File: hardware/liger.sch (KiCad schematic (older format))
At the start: 71 parts, among them P1 CONN_01X10, P2 CONN_01X10, P3 USB_OTG, P4 CONN_01X02, P5 CONN_01X04, Q1 Q_NMOS_GSD, Q2 Q_PMOS_GSD, Q3 Q_NPN_BEC, Q4 Q_NPN_BEC, SW1 SW_PUSH, U1 electret_microphone, U11 SPX3819, U2 ADA4075, U3 ESP-WROOM-02, U4 FT230XS, U5 PT5529B/L2/H2-F

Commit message: update
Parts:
- removed C?: 150nF, Capacitors_ThroughHole:C_Rect_L18_W6_H12_P15, symbol C
- removed R?: 1M, Resistors_ThroughHole:Resistor_Horizontal_RM15mm, symbol R
- removed R?: 68k, Resistors_ThroughHole:Resistor_Horizontal_RM15mm, symbol R
- removed R?: 33k, Resistors_ThroughHole:Resistor_Horizontal_RM15mm, symbol R
- removed R?: 6.8, Resistors_ThroughHole:Resistor_Horizontal_RM15mm, symbol R
- removed U?: common-mode-choke, symbol common-mode-choke
- added C? (x2): 12uF, Capacitors_ThroughHole:C_Radial_D10_L13_P5, symbol CP1
- added L?: BEAD, Resistors_SMD:R_0805_HandSoldering, symbol BK0603HS330-T
- added L?: 470uH, Capacitors_ThroughHole:C_Radial_D10_L13_P5, symbol BK0603HS330-T
- added R?: 0.91, Resistors_SMD:R_0805_HandSoldering, symbol R
- added R?: 0.82, Resistors_SMD:R_0805_HandSoldering, symbol R
- added RT?: 5, Resistors_ThroughHole:Resistor_Horizontal_RM10mm, symbol R
- BR?: renamed from D?; value Diode_Bridge -> DF08S; footprint (none) -> tba; Part Number (none) -> DF08S
- C?: value 150nF -> 330pF; footprint Capacitors_ThroughHole:C_Rect_L18_W6_H12_P15 -> Capacitors_SMD:C_0805_HandSoldering
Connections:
- wire segments 201 -> 200
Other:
- moved on the sheet: BR?, C?, D?

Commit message: update
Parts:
- C?: footprint Capacitors_ThroughHole:C_Radial_D16_L31.5_P7.5 -> Capacitors_ThroughHole:C_Radial_D10_L20_P7.5; Part Number (none) -> UPZ2G101MHD
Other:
- moved on the sheet: C?, D?
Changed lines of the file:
@@
 L C C?
 U 1 1 57C8658B
-P 5050 6650
-F 0 "C?" H 5150 6750 50  0000 L CNN
-F 1 "330pF" H 5100 6550 50  0000 L CNN
-F 2 "Capacitors_SMD:C_0805_HandSoldering" H 5165 6605 50  0001 L CNN
-F 3 "http://www.digikey.com/product-detail/en/kemet/C0805C331KCRACTU/399-7151-1-ND/3439391" H 5165 6514 50  0001 L CNN
-	1    5050 6650
+P 12400 7550
+F 0 "C?" H 12500 7650 50  0000 L CNN
+F 1 "330pF" H 12450 7450 50  0000 L CNN
+F 2 "Capacitors_SMD:C_0805_HandSoldering" H 12515 7505 50  0001 L CNN
+F 3 "http://www.digikey.com/product-detail/en/kemet/C0805C331KCRACTU/399-7151-1-ND/3439391" H 12515 7414 50  0001 L CNN
+	1    12400 7550
 	-1   0    0    1
 $EndComp
@@
 L CP1 C?
 U 1 1 57C87C6C
-P 8050 7600
-F 0 "C?" H 8165 7646 50  0000 L CNN
-F 1 "100uF" H 8165 7555 50  0000 L CNN
-F 2 "Capacitors_ThroughHole:C_Radial_D16_L31.5_P7.5" H 8165 7555 50  0001 L CNN
-F 3 "http://www.mouser.com/Search/ProductDetail.aspx?R=UPZ2G101MHDvirtualkey64700000virtualkey647-UPZ2G101MHD" H 8165 7464 50  0001 L CNN
-	1    8050 7600
+P 6250 8900
+F 0 "C?" H 6365 8946 50  0000 L CNN
+F 1 "100uF" H 6365 8855 50  0000 L CNN
+F 2 "Capacitors_ThroughHole:C_Radial_D10_L20_P7.5" H 6365 8855 50  0001 L CNN
+F 3 "http://www.mouser.com/Search/ProductDetail.aspx?R=UPZ2G101MHDvirtualkey64700000virtualkey647-UPZ2G101MHD" H 6365 8764 50  0001 L CNN
+F 4 "UPZ2G101MHD" H 6250 8900 60  0001 C CNN "Part Number"
+	1    6250 8900
 	1    0    0    -1
 $EndComp
@@
 L C C?
 U 1 1 57C8DD11
-P 8650 7050
-F 0 "C?" H 8750 7150 50  0000 L CNN
-F 1 "4.7nF" H 8700 6950 50  0000 L CNN
-F 2 "Capacitors_ThroughHole:C_Rect_L13_W4_P10" H 8765 7005 50  0001 L CNN
-F 3 "http://www.mouser.com/ProductDetail/EPCOS-TDK/B32641B0472K/?qs=sGAEpiMZZMv1cc3ydrPrFzRLALvOkyF1YTrqCCdx%2fGdcBMeHHlEFGg%3d%3d" H 8765 6914 50  0001 L CNN
-F 4 "B32641B0472K" H 8650 7050 60  0001 C CNN "Part Number"
-	1    8650 7050
+P 12400 7100
+F 0 "C?" H 12500 7200 50  0000 L CNN
+F 1 "4.7nF" H 12450 7000 50  0000 L CNN
+F 2 "Capacitors_ThroughHole:C_Rect_L13_W4_P10" H 12515 7055 50  0001 L CNN
+F 3 "http://www.mouser.com/ProductDetail/EPCOS-TDK/B32641B0472K/?qs=sGAEpiMZZMv1cc3ydrPrFzRLALvOkyF1YTrqCCdx%2fGdcBMeHHlEFGg%3d%3d" H 12515 6964 50  0001 L CNN
+F 4 "B32641B0472K" H 12400 7100 60  0001 C CNN "Part Number"
+	1    12400 7100
 	1    0    0    -1
 $EndComp
@@
 L D D?
 U 1 1 57C8E8E8
-P 8700 8200
-F 0 "D?" H 8700 8415 50  0000 C CNN
-F 1 "D" H 8700 8324 50  0000 C CNN
-F 2 "Diodes_SMD:SMB_Handsoldering" H 8700 8415 50  0001 C CNN
-F 3 "http://www.mouser.com/ProductDetail/Fairchild-Semiconductor/S1M/?qs=sGAEpiMZZMtbRapU8LlZD6Aoap19JQAxIRiMhMkksfk%3d" H 8700 8324 50  0001 C CNN
-F 4 "S1M" H 8700 8200 60  0001 C CNN "Part Number"
-	1    8700 8200
+P 12400 6800
+F 0 "D?" H 12400 7015 50  0000 C CNN
+F 1 "D" H 12400 6924 50  0000 C CNN
+F 2 "Diodes_SMD:SMB_Handsoldering" H 12400 7015 50  0001 C CNN
+F 3 "http://www.mouser.com/ProductDetail/Fairchild-Semiconductor/S1M/?qs=sGAEpiMZZMtbRapU8LlZD6Aoap19JQAxIRiMhMkksfk%3d" H 12400 6924 50  0001 C CNN
+F 4 "S1M" H 12400 6800 60  0001 C CNN "Part Number"
+	1    12400 6800
 	1    0    0    -1
 $EndComp

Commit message: yupdate
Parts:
- removed C7, C8: 47 pF, Capacitors_SMD:C_0402, symbol C
- removed C9: .1uF, Capacitors_SMD:C_0603, symbol C
- removed D5, D6, D7: LED, LEDs:LED_0603, symbol LED
- removed FB1: BK1608HS330-T, Resistors_SMD:R_0603, symbol BK0603HS330-T
- removed P3: USB_OTG, footprints:USB_Micro-B_CIRC, symbol USB_OTG
- removed R15, R16: 27K, Resistors_SMD:R_0603, symbol R
- removed R18, R20, R21, R22, R23: 1K, Resistors_SMD:R_0603, symbol R
- removed U4: FT230XS, Housings_SSOP:SSOP-16_3.9x4.9mm_Pitch0.635mm, symbol FT230XS
- gave numbers to parts that had none: 12
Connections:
- net labels removed: DM, DP, USB_Controller
- wire segments 200 -> 149

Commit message: update
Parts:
- BR1: footprint tba -> Diodes_ThroughHole:Diode_Bridge_15.7x15.7
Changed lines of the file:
@@
 F 0 "BR1" H 3250 9550 50  0000 L CNN
 F 1 "DF08S" H 3000 9550 50  0001 L CNN
-F 2 "tba" H 3600 9250 50  0001 C CNN
+F 2 "Diodes_ThroughHole:Diode_Bridge_15.7x15.7" H 3600 9250 50  0001 C CNN
 F 3 "http://www.digikey.com/scripts/DkSearch/dksus.dll?Detail&itemSeq=206259955&uq=636087571188496593" H 3600 9250 50  0001 C CNN
 F 4 "DF08S" H 3600 9250 60  0001 C CNN "Part Number"

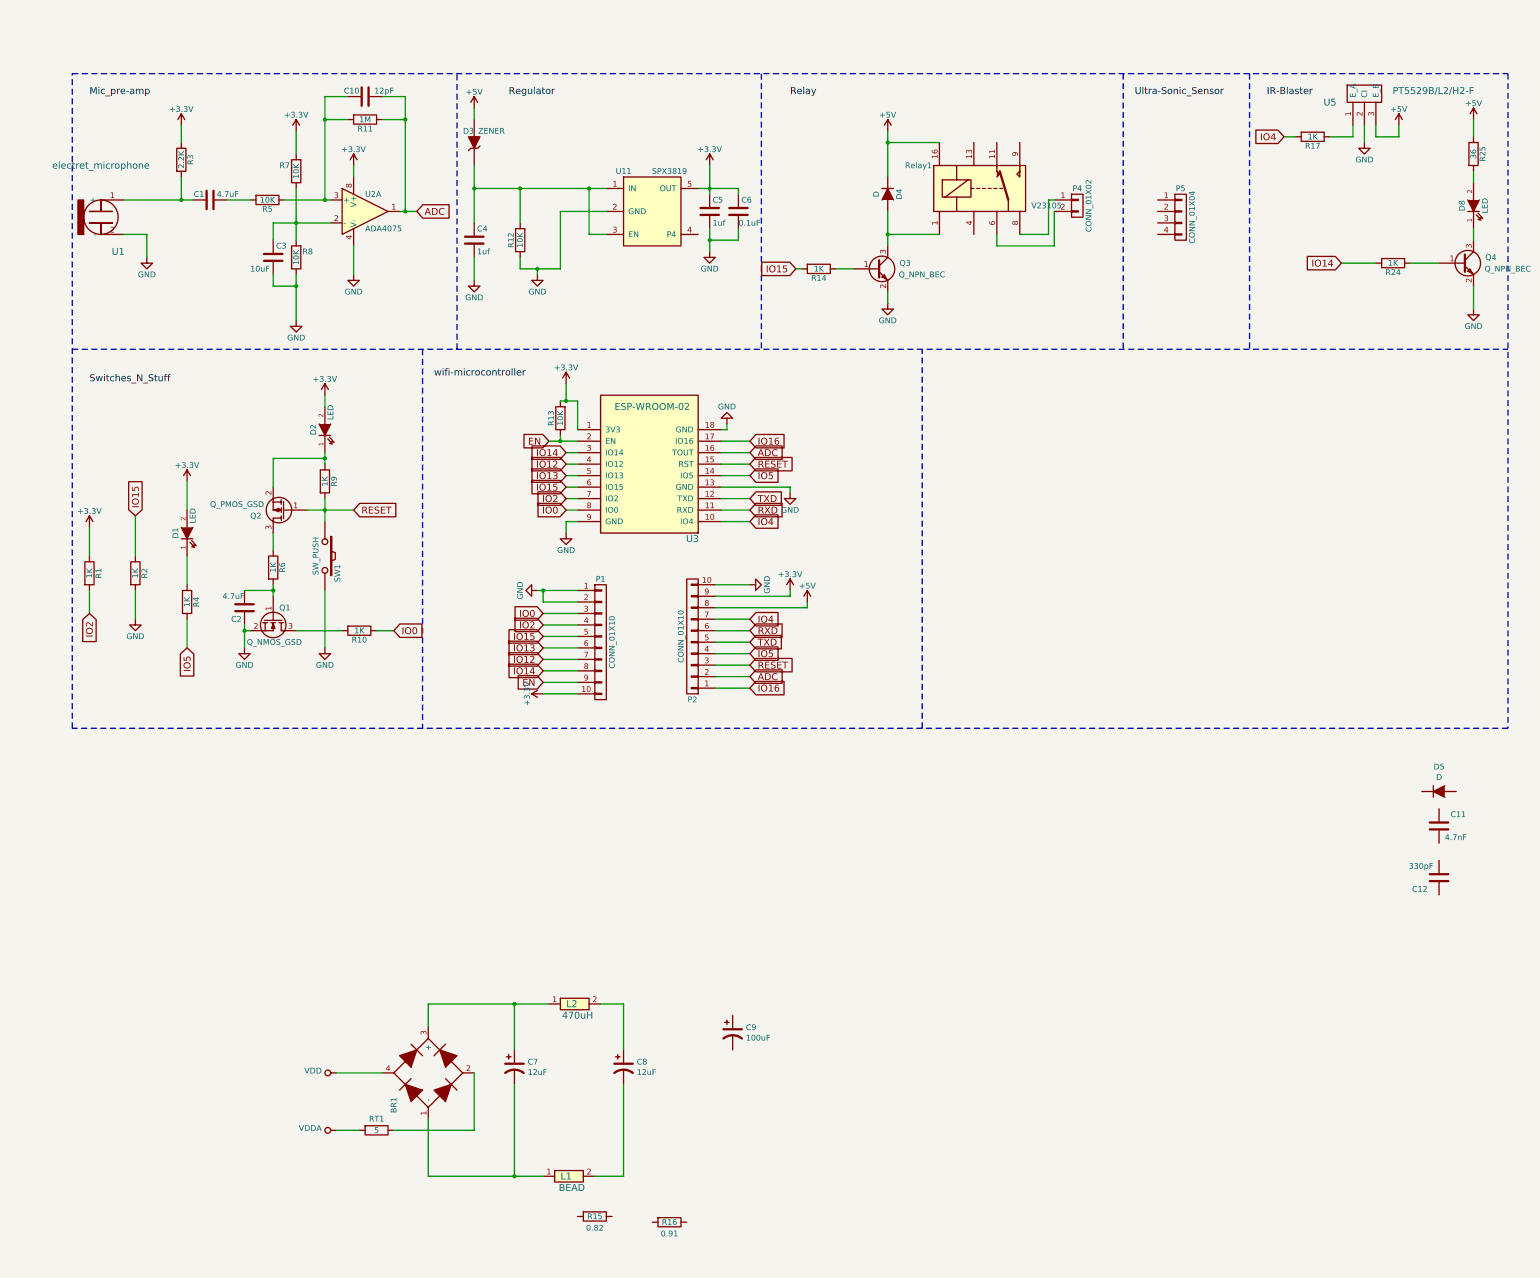
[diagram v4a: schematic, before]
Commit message: added MEMS mic
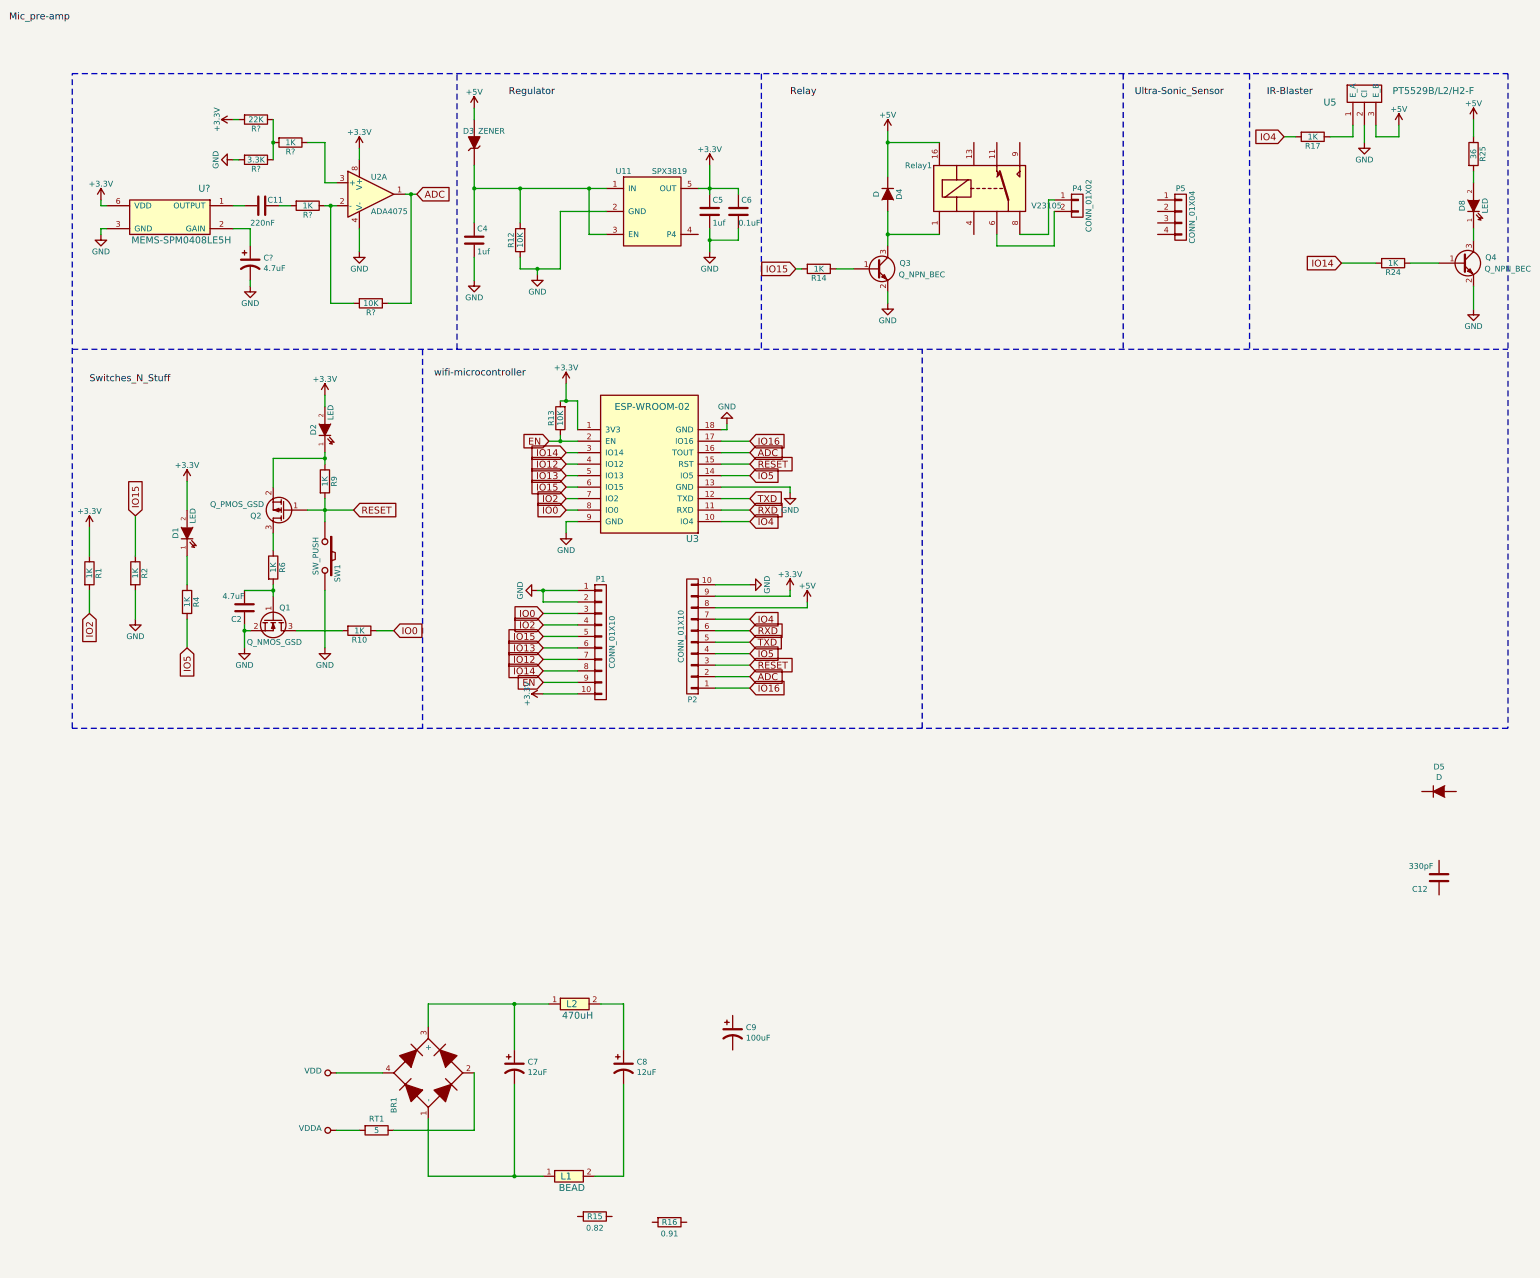
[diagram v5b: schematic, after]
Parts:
- removed C1: 4.7uF, Capacitors_SMD:C_0603, symbol C
- removed C10: 12pF, Capacitors_SMD:C_0402, symbol C
- removed C3: 10uF, Capacitors_SMD:C_0603, symbol C
- removed R11: 1M, Resistors_SMD:R_0603, symbol R
- removed R3: 2.2K, Resistors_SMD:R_0603, symbol R
- removed R5, R7, R8: 10K, Resistors_SMD:R_0603, symbol R
- removed U1: electret_microphone, libraries:Electret, symbol electret_microphone
- added C?: 4.7uF, Capacitors_ThroughHole:C_Radial_D10_L13_P5, symbol CP1
- added R? (x2): 1K, Resistors_SMD:R_0603, symbol R
- added R?: 10K, Resistors_SMD:R_0603, symbol R
- added R?: 22K, Resistors_SMD:R_0603, symbol R
- added R?: 3.3K, Resistors_SMD:R_0603, symbol R
- added U?: MEMS-SPM0408LE5H, symbol MEMS-SPM0408LE5H
- C11: value 4.7nF -> 220nF
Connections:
- net +3V3: now also R?.2, U?.6 (VDD)
- net ADC: now also R?.1
- net GND: now also C?.2, R?.2, U?.3 (GND)
- net at U2.3 (+): now also R?.1
- net at U2.2 (-): now also R?.1, R?.2
- net at C11.1: now also R?.2
- net at C11.2: now also U?.1 (OUTPUT)
- new net: C?.1, U?.2 (GAIN)
- new net: R?.1, R?.1, R?.2
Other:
- moved on the sheet: C11, U2A

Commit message: update
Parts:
- removed R? (x2): 1K, Resistors_SMD:R_0603, symbol R
- removed R?: 10K, Resistors_SMD:R_0603, symbol R
- added C? (x4): 330pF, Capacitors_SMD:C_0805_HandSoldering, symbol C
- added C?: 100uF, Capacitors_ThroughHole:C_Radial_D10_L20_P7.5, symbol CP1
- added D? (x3): D, Diodes_SMD:SMB_Handsoldering, symbol D
- added Q?: Q_NPN_BEC, TO_SOT_Packages_SMD:SOT-23, symbol Q_NPN_BEC
- added R? (x2): 1K, Resistors_SMD:R_0603, symbol R
- added R?: 10K, Resistors_SMD:R_0603, symbol R
- added R? (x2): 270, Resistors_SMD:R_0805_HandSoldering, symbol R
- added R? (x9): 27M, Resistors_SMD:R_0805_HandSoldering, symbol R
- added R?: 5.1K, Resistors_SMD:R_0805_HandSoldering, symbol R
- added U?: LNK4023D, symbol LNK4023D
- added U?: EPC1716D, symbol EPC1716D
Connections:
- net +5V: now also C9.1, C?.1, C?.1, D?.1 (K), D?.1 (K), R?.2
- net ADC: now also R?.2
- net GND: now also C9.2, C?.2, C?.2, R?.1, U?.6 (SEC-)
- net at U2.2 (-): now also R?.1, R?.1
- net at U2.3 (+): now also R?.1
- net at C12.1: now also D?.1 (K), R?.2
- net at C12.2: now also C8.1, L2.2, C?.1, R?.1, R?.1, U?.3 (PRI2-)
- net at C11.1: now also R?.2
- net at D5.1 (K): now also R?.1
- net at D5.2 (A): now also R?.1, U?.2 (AUX+)
- net at C8.2, L1.2: now also R15.2, R16.2, R?.1
- net at R16.1: now also R15.1, C?.2, C?.2, R?.2, U?.1 (AUX-), U?.6 (GND)
- net at R?.1, R?.1: now also R?.2
- new net: R?.2, U?.1 (CS)
- new net: C?.1, C?.1, R?.2, R?.2, U?.2 (VCC)
- new net: R?.1, U?.3 (SBD)
- new net: Q?.1 (B), R?.2, U?.3 (SBD)
- new net: Q?.2 (E), U?.5 (ED)
- new net: R?.1, R?.2, U?.8 (FB)
- new net: R?.1, R?.2 (x2)
- new net: Q?.3 (C), R?.2, U?.5 (PRI1)
- new net: D?.2 (A), R?.1
- new net: D?.2 (A), D?.2 (A), R?.2, U?.7 (SEC+)
- new net: C?.2, R?.1
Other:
- moved on the sheet: C12, C9, D5, R15, R16

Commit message: update
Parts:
- removed D3: ZENER, Diodes_SMD:SOD-123, symbol ZENER
- C9, C?: value 100uF -> 560uF
- C?: value 330pF -> 100pF
- C?: value 330pF -> 2.2uF
- C?: value 330pF -> 2.2pF
- C?: value 330pF -> 1000pF
- R1, R10, R12, R13, R14, R17, R2, R24, R25, R4, R6, R9, R? (x5): footprint Resistors_SMD:R_0603 -> Resistors_SMD:R_0603_HandSoldering
- R15, R16, R? (x6): footprint Resistors_SMD:R_0805_HandSoldering -> Resistors_SMD:R_0603_HandSoldering
- R?: value 27M -> 300; footprint Resistors_SMD:R_0805_HandSoldering -> Resistors_SMD:R_0603_HandSoldering
- R?: value 27M -> 3K; footprint Resistors_SMD:R_0805_HandSoldering -> Resistors_SMD:R_0603_HandSoldering
- R?: value 27M -> 620; footprint Resistors_SMD:R_0805_HandSoldering -> Resistors_SMD:R_0603_HandSoldering
- R?: value 27M -> 9.1K; footprint Resistors_SMD:R_0805_HandSoldering -> Resistors_SMD:R_0603_HandSoldering
- R?: value 27M -> 1; footprint Resistors_SMD:R_0805_HandSoldering -> Resistors_SMD:R_0603_HandSoldering
- R?: value 27M -> 4.7; footprint Resistors_SMD:R_0805_HandSoldering -> Resistors_SMD:R_0603_HandSoldering
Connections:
- net +5V: now also C4.1, R12.2, U11.1 (IN), U11.3 (EN)

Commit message: update
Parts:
- removed C?: 4.7uF, Capacitors_ThroughHole:C_Radial_D10_L13_P5, symbol CP1
- removed R?: 1K, Resistors_SMD:R_0603_HandSoldering, symbol R
- added C?: 4.7uf, Capacitors_SMD:C_0603_HandSoldering, symbol C
- added R?: 1K, Resistors_SMD:R_0603_HandSoldering, symbol R
- C11: footprint Capacitors_ThroughHole:C_Rect_L13_W4_P10 -> Capacitors_SMD:C_0603_HandSoldering; Part Number B32641B0472K -> C1608X7R1C224K080AC
- R?: Part Number RC0603FR-072K2L -> RC0603JR-0722KL
- R?: Part Number RC0603FR-072K2L -> RC0603JR-073K3L
- U2: footprint Housings_SOIC:SOIC-8_3.9x4.9mm_Pitch1.27mm -> TO_SOT_Packages_SMD:SOT-23-5
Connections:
- net GND: now also C?.1
- net at R?.1, U2.2 (-): now also R?.1
- net at C11.1: now also R?.2
- net at U?.2 (GAIN): now also C?.2
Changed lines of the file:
@@
 F 0 "U2" H 3100 1750 50  0000 L CNN
 F 1 "ADA4075" H 3100 1450 50  0000 L CNN
-F 2 "Housings_SOIC:SOIC-8_3.9x4.9mm_Pitch1.27mm" H 3000 1650 50  0001 C CNN
-F 3 "http://www.mouser.com/ds/2/609/OP275-879536.pdf" H 3100 1750 50  0001 C CNN
+F 2 "TO_SOT_Packages_SMD:SOT-23-5" H 3000 1650 50  0001 C CNN
+F 3 "http://www.digikey.com/product-detail/en/texas-instruments/OPA344NA-3K/296-41475-1-ND/5222851" H 3100 1750 50  0001 C CNN
 F 4 "OPA344NA/3K" H 3100 1600 60  0001 C CNN "Part Number"
 	1    3100 1600
@@
 Text Label 4300 750  0    60   ~ 0
 Regulator
-Text Label -50  100  0    60   ~ 0
+Text Label 550  700  0    60   ~ 0
 Mic_pre-amp
 $Comp
@@
 F 0 "C11" V 2100 1750 50  0000 L CNN
 F 1 "220nF" V 2300 1600 50  0000 L CNN
-F 2 "Capacitors_ThroughHole:C_Rect_L13_W4_P10" H 2265 1655 50  0001 L CNN
-F 3 "http://www.mouser.com/ProductDetail/EPCOS-TDK/B32641B0472K/?qs=sGAEpiMZZMv1cc3ydrPrFzRLALvOkyF1YTrqCCdx%2fGdcBMeHHlEFGg%3d%3d" H 2265 1564 50  0001 L CNN
-F 4 "B32641B0472K" H 2150 1700 60  0001 C CNN "Part Number"
+F 2 "Capacitors_SMD:C_0603_HandSoldering" H 2265 1655 50  0001 L CNN
+F 3 "http://www.digikey.com/product-detail/en/tdk-corporation/C1608X7R1C224K080AC/445-1318-1-ND/567690" H 2265 1564 50  0001 L CNN
+F 4 "C1608X7R1C224K080AC" H 2150 1700 60  0001 C CNN "Part Number"
 	1    2150 1700
 	0    1    1    0
@@
 F 2 "Resistors_SMD:R_0603_HandSoldering" V 2030 950 50  0001 C CNN
 F 3 "http://www.digikey.com/en/resources/datasheets/yageo/rc-series-l-suffix-datasheet" H 2100 950 50  0001 C CNN
-F 4 "RC0603FR-072K2L" V 2100 950 60  0001 C CNN "Part Number"
+F 4 "RC0603JR-0722KL" V 2100 950 60  0001 C CNN "Part Number"
 	1    2100 950
 	0    1    1    0
@@
 F 1 "3.3K" V 2100 1300 50  0000 C CNN
 F 2 "Resistors_SMD:R_0603_HandSoldering" V 2030 1300 50  0001 C CNN
-F 3 "http://www.digikey.com/en/resources/datasheets/yageo/rc-series-l-suffix-datasheet" H 2100 1300 50  0001 C CNN
-F 4 "RC0603FR-072K2L" V 2100 1300 60  0001 C CNN "Part Number"
+F 3 "http://www.digikey.com/product-detail/en/yageo/RC0603JR-073K3L/311-3.3KGRCT-ND/729704" H 2100 1300 50  0001 C CNN
+F 4 "RC0603JR-073K3L" V 2100 1300 60  0001 C CNN "Part Number"
 	1    2100 1300
 	0    1    1    0
@@
 $EndComp
 $Comp
-L CP1 C?
-U 1 1 57D112C9
-P 2050 2200
-F 0 "C?" H 2165 2246 50  0000 L CNN
-F 1 "4.7uF" H 2165 2155 50  0000 L CNN
-F 2 "Capacitors_ThroughHole:C_Radial_D10_L13_P5" H 2165 2155 50  0001 L CNN
-F 3 "http://www.digikey.com/product-detail/en/rubycon/400AX12MEFC10X12.5/1189-3120-ND/6049840" H 2165 2064 50  0001 L CNN
-	1    2050 2200
-	1    0    0    -1
-$EndComp
-$Comp
 L GND #PWR?
 U 1 1 57D13092
@@
 	1    2050 2400
 	1    0    0    -1
-$EndComp
-$Comp
-L R R?
-U 1 1 57D1D2C5
-P 2550 1700
-F 0 "R?" V 2630 1700 50  0000 C CNN
-F 1 "1K" V 2550 1700 50  0000 C CNN
-F 2 "Resistors_SMD:R_0603_HandSoldering" V 2480 1700 50  0001 C CNN
-F 3 "http://www.digikey.com/en/resources/datasheets/yageo/rc-series-l-suffix-datasheet" H 2550 1700 50  0001 C CNN
-F 4 "RC0603JR-071KL" V 2550 1700 60  0001 C CNN "Part Number"
-	1    2550 1700
-	0    1    1    0
 $EndComp
 $Comp
@@
 F 1 "1K" V 2400 1150 50  0000 C CNN
 F 2 "Resistors_SMD:R_0603_HandSoldering" V 2330 1150 50  0001 C CNN
-F 3 "http://www.digikey.com/en/resources/datasheets/yageo/rc-series-l-suffix-datasheet" H 2400 1150 50  0001 C CNN
+F 3 "http://www.digikey.com/product-detail/en/yageo/RC0603JR-071KL/311-1.0KGRCT-ND/729624" H 2400 1150 50  0001 C CNN
 F 4 "RC0603JR-071KL" V 2400 1150 60  0001 C CNN "Part Number"
 	1    2400 1150
@@
 	1    0    0    -1
 $EndComp
+$Comp
+L C C?
+U 1 1 57D31D9B
+P 2050 2200
+F 0 "C?" V 2000 2250 50  0000 L CNN
+F 1 "4.7uf" V 2200 2100 50  0000 L CNN
+F 2 "Capacitors_SMD:C_0603_HandSoldering" H 2165 2155 50  0001 L CNN
+F 3 "http://www.digikey.com/product-detail/en/samsung-electro-mechanics-america-inc/CL10B475KQ8NQNC/1276-2087-1-ND/3890173" H 2165 2064 50  0001 L CNN
+F 4 "CL10B475KQ8NQNC" H 2050 2200 60  0001 C CNN "Part Number"
+	1    2050 2200
+	-1   0    0    1
+$EndComp
+$Comp
+L R R?
+U 1 1 57D32F11
+P 2550 1700
+F 0 "R?" V 2630 1700 50  0000 C CNN
+F 1 "1K" V 2550 1700 50  0000 C CNN
+F 2 "Resistors_SMD:R_0603_HandSoldering" V 2480 1700 50  0001 C CNN
+F 3 "http://www.digikey.com/product-detail/en/yageo/RC0603JR-071KL/311-1.0KGRCT-ND/729624" H 2550 1700 50  0001 C CNN
+F 4 "RC0603JR-071KL" V 2550 1700 60  0001 C CNN "Part Number"
+	1    2550 1700
+	0    1    1    0
+$EndComp
 $EndSCHEMATC
